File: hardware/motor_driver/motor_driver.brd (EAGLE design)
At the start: 93.7 x 72.4 mm, 88 parts

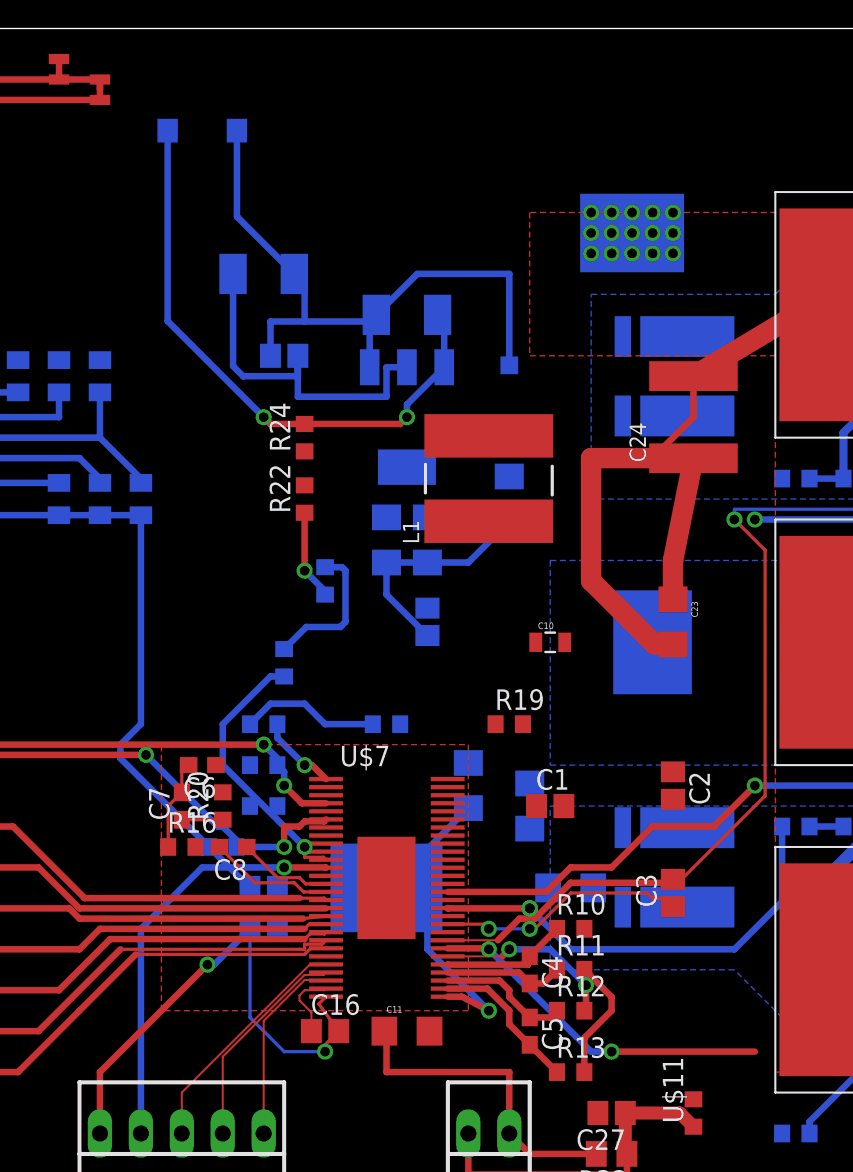
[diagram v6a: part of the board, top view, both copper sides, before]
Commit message: Fixed some of the spacing issues aroud the Driver
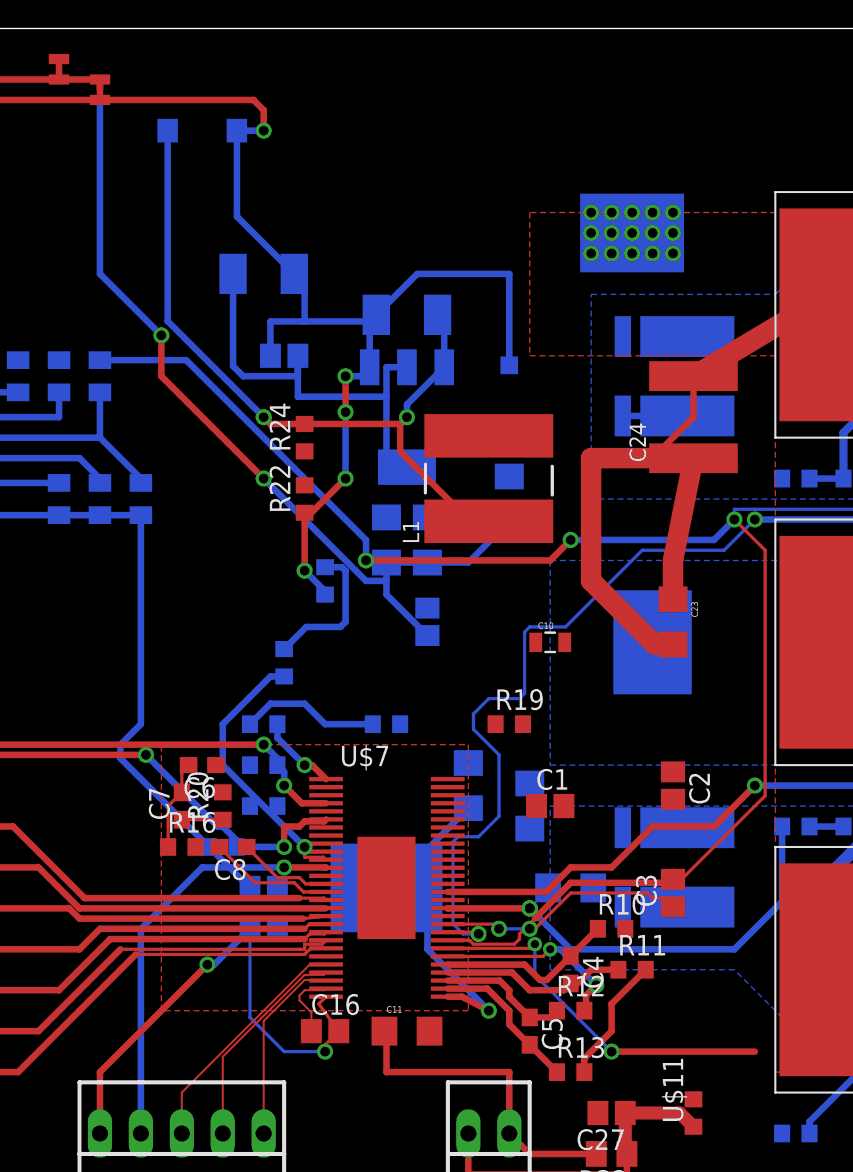
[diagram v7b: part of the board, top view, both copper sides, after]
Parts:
- moved R11 3.81 mm to (58.4, 14.0)
- moved C4 2.54 mm to (54.6, 14.0)
- moved R10 2.54 mm to (57.1, 16.5)
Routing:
- net H3_VS: track 74.6 -> 121.5 mm, vias 2 -> 4
- net GH_C: track 25.2 -> 69.3 mm, vias 1 -> 2
- net GND: track 34.1 -> 72.2 mm, vias 0 -> 2
- net DGND: track 135.6 -> 160.4 mm, vias 1 -> 5
- net +5V: track 37.0 -> 46.0 mm
- net +3V3: track 22.4 -> 28.5 mm
- net H3_LOW: track 11.3 -> 16.2 mm
- net N$23: track 7.41 -> 11.6 mm
- net N$22: track 7.92 -> 11.0 mm
- net GL_C: track 21.7 -> 23.0 mm

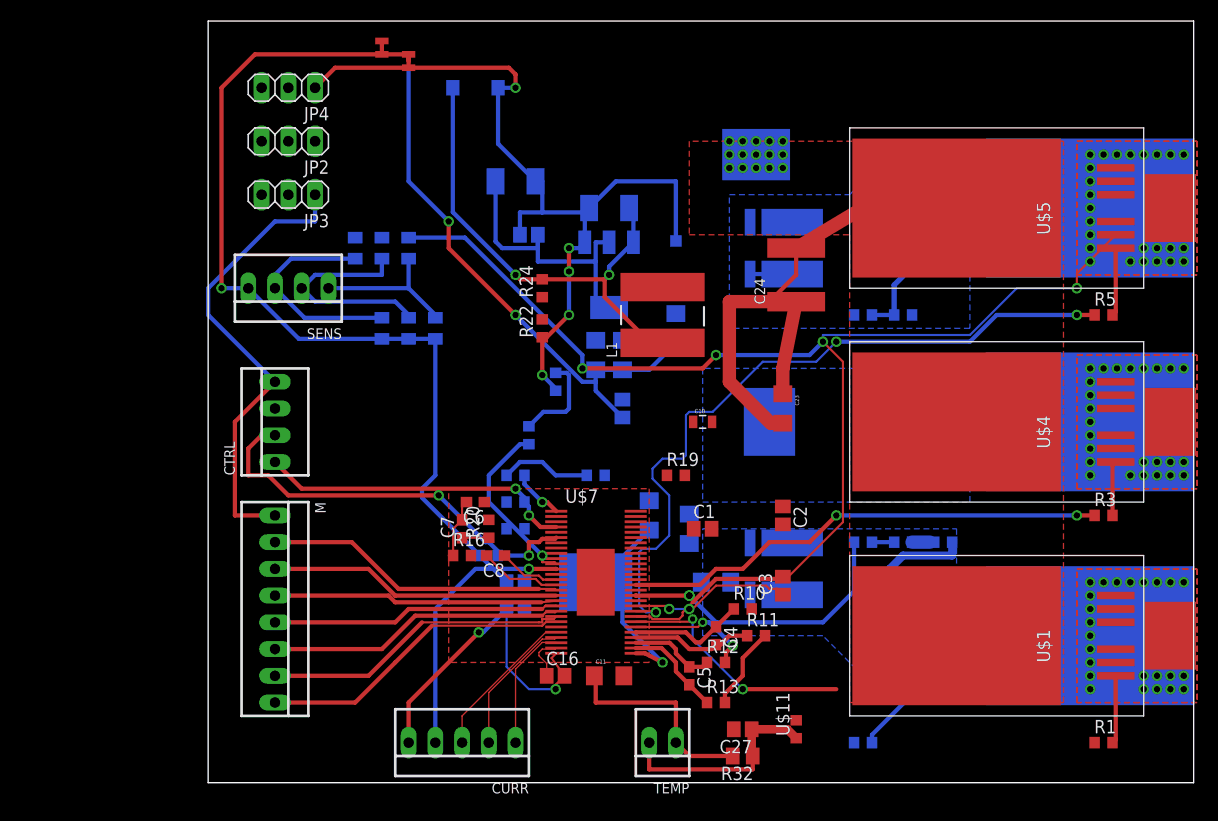
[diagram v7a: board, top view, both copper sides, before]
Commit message: Changed shunt resistor sch, needs confirmtion
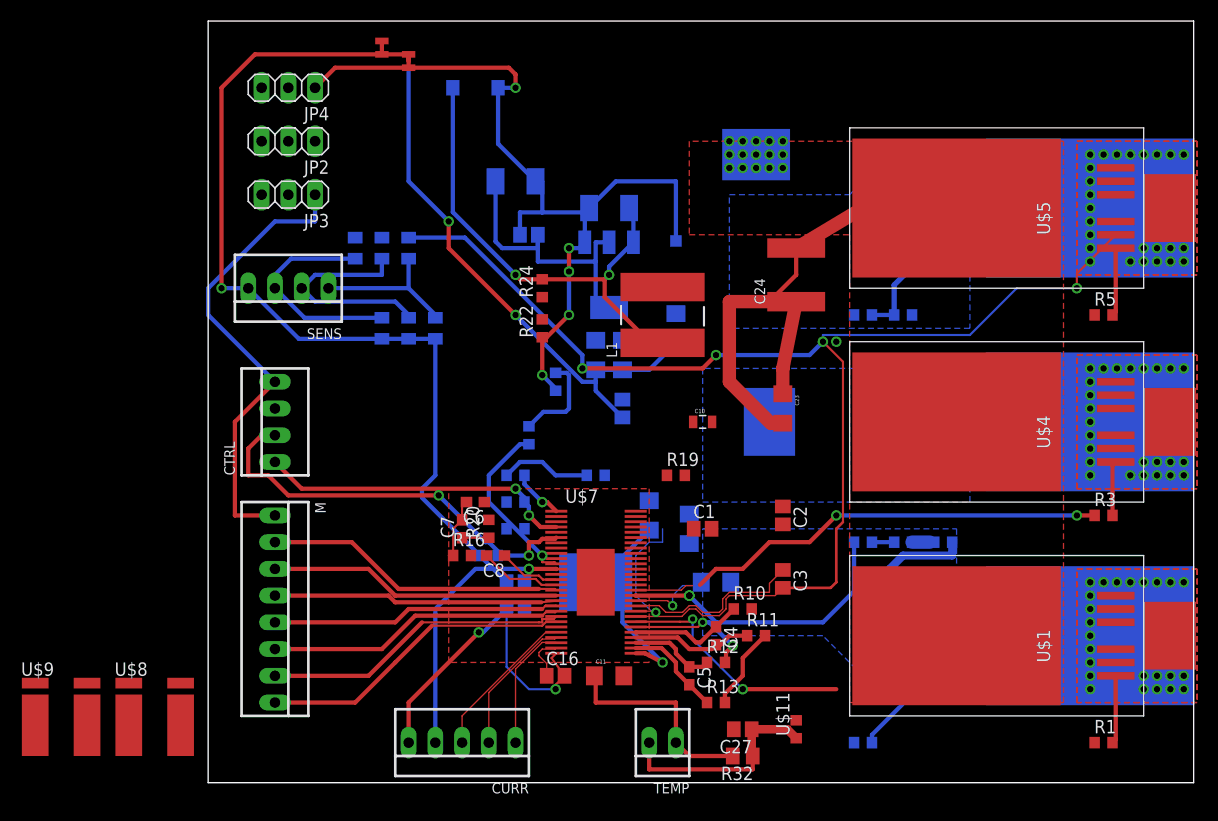
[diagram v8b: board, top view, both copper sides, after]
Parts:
- moved U$9 81.7 mm to (-7.62, 6.35), flipped to the top, turned to 0 degrees
- moved U$8 61.3 mm to (1.27, 6.35), flipped to the top, turned to 0 degrees
- moved C3 0.63 mm to (61.0, 19.4), turned to 270 degrees
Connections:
- net GND: now also U$8.P$4; no longer U$8.P$1@1, U$8.P$1@2, U$9.P$1@1, U$9.P$1@2
- net H1_LOW: now also U$8.P$1; no longer U$8.P$2@1, U$8.P$2@2
- net H3_LOW: now also U$9.P$1; no longer U$9.P$2@1, U$9.P$2@2
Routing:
- net GH_C: track 69.3 -> 12.7 mm, vias 2 -> 1
- net GND: track 72.2 -> 80.1 mm, vias 2 -> 3
- net GH_B: track 46.3 -> 40.2 mm
- net H2_VS: track 0.00 -> 5.73 mm
- net H3_LOW: track 16.2 -> 12.2 mm
- net H3_VS: track 121.5 -> 124.9 mm
- net N$26: track 15.4 -> 17.5 mm, vias 2 -> 0
